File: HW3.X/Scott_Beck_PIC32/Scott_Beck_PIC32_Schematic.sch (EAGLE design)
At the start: 22 parts, among them J1 USB-MB-H

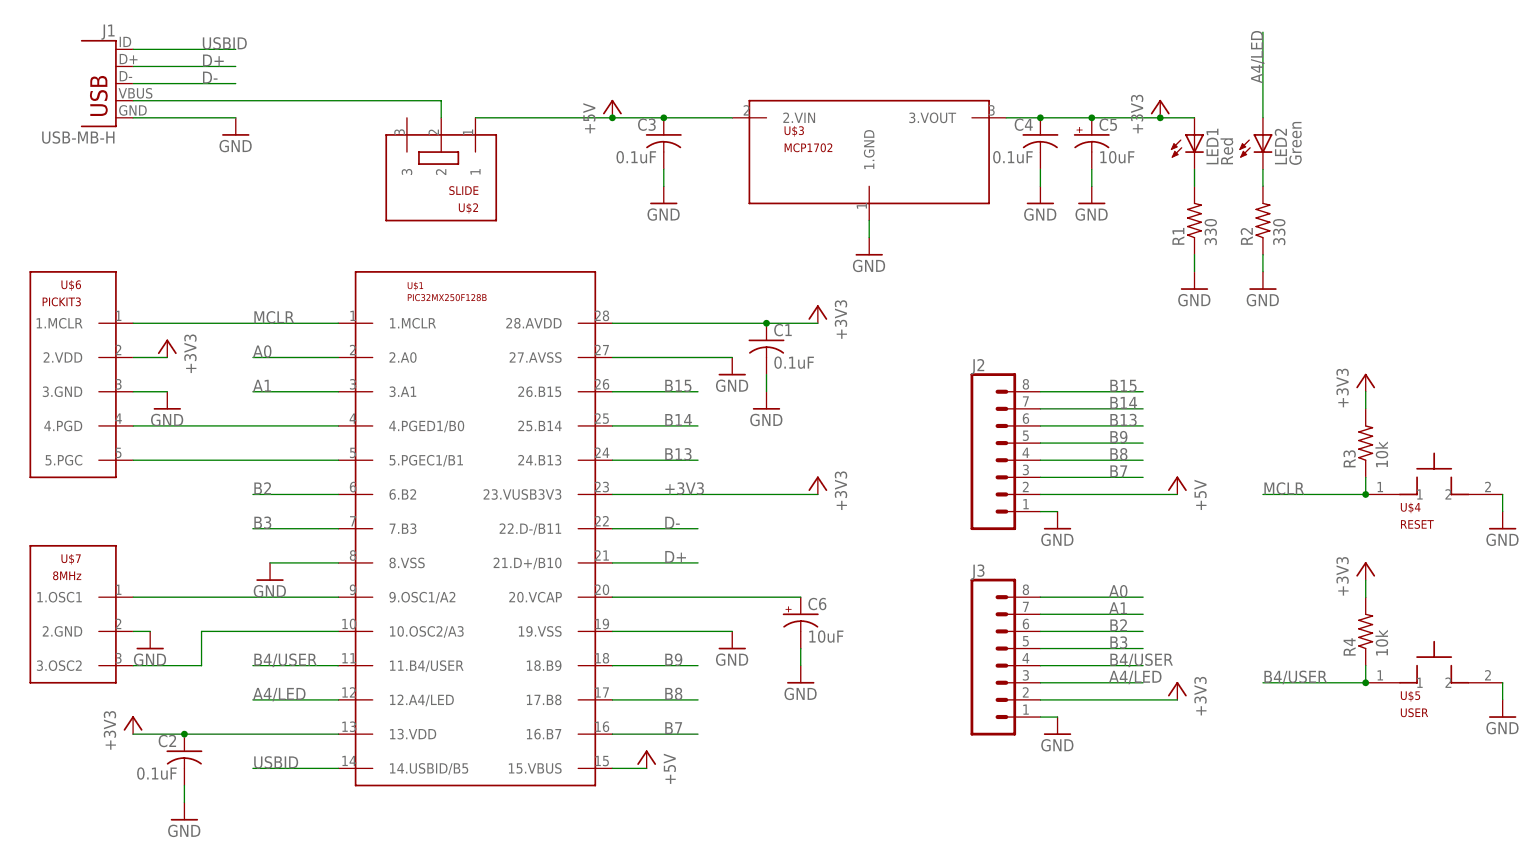
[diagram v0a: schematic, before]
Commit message: Updated Board
Began Design, Replaced res/cap with surface mounts.
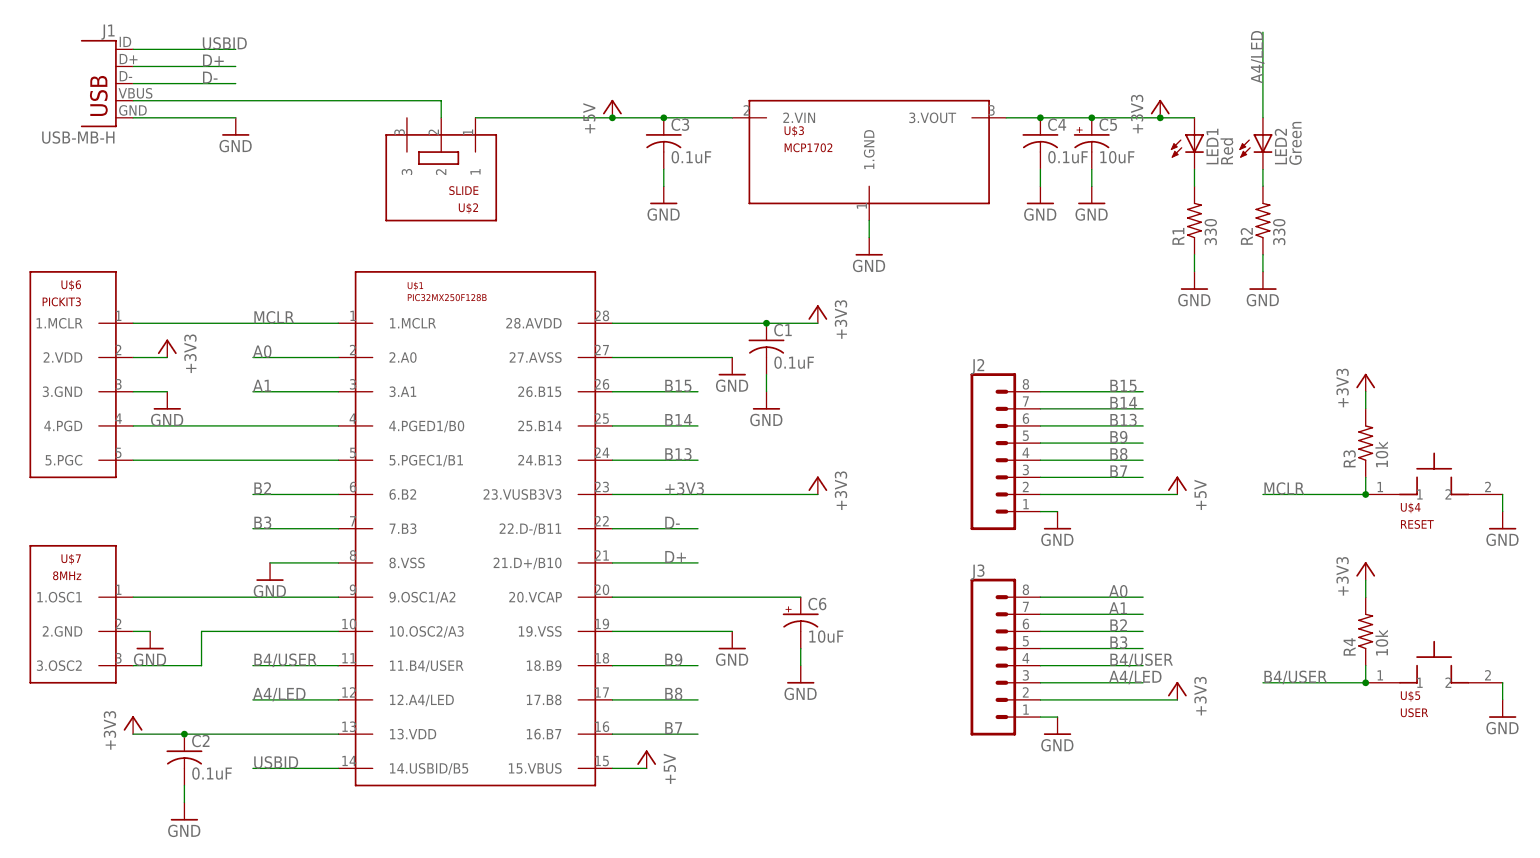
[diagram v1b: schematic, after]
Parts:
- C1, C2, C3, C4: device Scott_Beck_PIC32_Library:C-US025-025X050 -> resistor:C-USC0603
- R1, R2, R3, R4: device Scott_Beck_PIC32_Library:R-US_0207/10 -> resistor:R-US_R0603
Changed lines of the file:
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@@
 <part name="U$4" library="Scott_Beck_PIC32_Library" deviceset="PB" device="" value="RESET"/>
 <part name="U$5" library="Scott_Beck_PIC32_Library" deviceset="PB" device="" value="USER"/>
-<part name="R1" library="Scott_Beck_PIC32_Library" deviceset="R-US_" device="0207/10" value="330"/>
-<part name="R2" library="Scott_Beck_PIC32_Library" deviceset="R-US_" device="0207/10" value="330"/>
-<part name="R3" library="Scott_Beck_PIC32_Library" deviceset="R-US_" device="0207/10" value="10k"/>
-<part name="R4" library="Scott_Beck_PIC32_Library" deviceset="R-US_" device="0207/10" value="10k"/>
-<part name="C1" library="Scott_Beck_PIC32_Library" deviceset="C-US" device="025-025X050" value="0.1uF"/>
-<part name="C2" library="Scott_Beck_PIC32_Library" deviceset="C-US" device="025-025X050" value="0.1uF"/>
-<part name="C3" library="Scott_Beck_PIC32_Library" deviceset="C-US" device="025-025X050" value="0.1uF"/>
-<part name="C4" library="Scott_Beck_PIC32_Library" deviceset="C-US" device="025-025X050" value="0.1uF"/>
 <part name="C5" library="Scott_Beck_PIC32_Library" deviceset="CPOL-US" device="B45181B" value="10uF"/>
 <part name="C6" library="Scott_Beck_PIC32_Library" deviceset="CPOL-US" device="B45181B" value="10uF"/>
@@
 <part name="+3V8" library="Scott_Beck_PIC32_Library" deviceset="+3V3" device=""/>
 <part name="GND19" library="Scott_Beck_PIC32_Library" deviceset="GND" device=""/>
+<part name="R1" library="resistor" deviceset="R-US_" device="R0603" value="330"/>
+<part name="R3" library="resistor" deviceset="R-US_" device="R0603" value="10k"/>
+<part name="R2" library="resistor" deviceset="R-US_" device="R0603" value="330"/>
+<part name="R4" library="resistor" deviceset="R-US_" device="R0603" value="10k"/>
+<part name="C1" library="resistor" deviceset="C-US" device="C0603" value="0.1uF"/>
+<part name="C2" library="resistor" deviceset="C-US" device="C0603" value="0.1uF"/>
+<part name="C3" library="resistor" deviceset="C-US" device="C0603" value="0.1uF"/>
+<part name="C4" library="resistor" deviceset="C-US" device="C0603" value="0.1uF"/>
 </parts>
 <sheets>
@@
 <instance part="U$4" gate="G$1" x="76.2" y="12.7"/>
 <instance part="U$5" gate="G$1" x="76.2" y="-15.24"/>
-<instance part="R1" gate="G$1" x="40.64" y="53.34" rot="R90"/>
-<instance part="R2" gate="G$1" x="50.8" y="53.34" rot="R90"/>
-<instance part="R3" gate="G$1" x="66.04" y="20.32" rot="R90"/>
-<instance part="R4" gate="G$1" x="66.04" y="-7.62" rot="R90"/>
-<instance part="C1" gate="G$1" x="-22.86" y="35.56"/>
-<instance part="C2" gate="G$1" x="-109.22" y="-25.4" rot="MR0"/>
-<instance part="C3" gate="G$1" x="-38.1" y="66.04" rot="MR0"/>
-<instance part="C4" gate="G$1" x="17.78" y="66.04" rot="MR0"/>
 <instance part="C5" gate="G$1" x="25.4" y="66.04"/>
 <instance part="C6" gate="G$1" x="-17.78" y="-5.08"/>
@@
 <instance part="+3V8" gate="G$1" x="66.04" y="2.54"/>
 <instance part="GND19" gate="1" x="50.8" y="43.18"/>
+<instance part="R1" gate="G$1" x="40.64" y="53.34" rot="R90"/>
+<instance part="R3" gate="G$1" x="66.04" y="20.32" rot="R90"/>
+<instance part="R2" gate="G$1" x="50.8" y="53.34" rot="R90"/>
+<instance part="R4" gate="G$1" x="66.04" y="-7.62" rot="R90"/>
+<instance part="C1" gate="G$1" x="-22.86" y="35.56"/>
+<instance part="C2" gate="G$1" x="-109.22" y="-25.4"/>
+<instance part="C3" gate="G$1" x="-38.1" y="66.04"/>
+<instance part="C4" gate="G$1" x="17.78" y="66.04"/>
 </instances>
 <busses>
@@
 <net name="GND" class="0">
 <segment>
-<pinref part="C1" gate="G$1" pin="2"/>
 <pinref part="GND8" gate="1" pin="GND"/>
 <wire x1="-22.86" y1="27.94" x2="-22.86" y2="30.48" width="0.1524" layer="91"/>
+<pinref part="C1" gate="G$1" pin="2"/>
 </segment>
 <segment>
@@
 </segment>
 <segment>
-<pinref part="C3" gate="G$1" pin="2"/>
 <pinref part="GND10" gate="1" pin="GND"/>
 <wire x1="-38.1" y1="60.96" x2="-38.1" y2="58.42" width="0.1524" layer="91"/>
+<pinref part="C3" gate="G$1" pin="2"/>
 </segment>
 <segment>
@@
 </segment>
 <segment>
-<pinref part="C4" gate="G$1" pin="2"/>
 <pinref part="GND11" gate="1" pin="GND"/>
 <wire x1="17.78" y1="60.96" x2="17.78" y2="58.42" width="0.1524" layer="91"/>
+<pinref part="C4" gate="G$1" pin="2"/>
 </segment>
 <segment>
@@
 </segment>
 <segment>
-<pinref part="R1" gate="G$1" pin="1"/>
 <pinref part="GND14" gate="1" pin="GND"/>
 <wire x1="40.64" y1="48.26" x2="40.64" y2="45.72" width="0.1524" layer="91"/>
+<pinref part="R1" gate="G$1" pin="1"/>
 </segment>
 <segment>
@@
 </segment>
 <segment>
-<pinref part="C2" gate="G$1" pin="2"/>
 <pinref part="GND4" gate="1" pin="GND"/>
 <wire x1="-109.22" y1="-30.48" x2="-109.22" y2="-33.02" width="0.1524" layer="91"/>
+<pinref part="C2" gate="G$1" pin="2"/>
 </segment>
 <segment>
@@
 </segment>
 <segment>
-<pinref part="R2" gate="G$1" pin="1"/>
 <pinref part="GND19" gate="1" pin="GND"/>
 <wire x1="50.8" y1="48.26" x2="50.8" y2="45.72" width="0.1524" layer="91"/>
+<pinref part="R2" gate="G$1" pin="1"/>
 </segment>
 </net>
@@
 <pinref part="P+1" gate="1" pin="+5V"/>
 <wire x1="-66.04" y1="68.58" x2="-45.72" y2="68.58" width="0.1524" layer="91"/>
-<pinref part="C3" gate="G$1" pin="1"/>
-<wire x1="-38.1" y1="68.58" x2="-45.72" y2="68.58" width="0.1524" layer="91"/>
 <junction x="-45.72" y="68.58"/>
 <pinref part="U$3" gate="G$1" pin="2.VIN"/>
+<wire x1="-45.72" y1="68.58" x2="-38.1" y2="68.58" width="0.1524" layer="91"/>
+<pinref part="C3" gate="G$1" pin="1"/>
 <wire x1="-38.1" y1="68.58" x2="-27.94" y2="68.58" width="0.1524" layer="91"/>
 <junction x="-38.1" y="68.58"/>
@@
 <segment>
 <pinref part="U$3" gate="G$1" pin="3.VOUT"/>
-<pinref part="C4" gate="G$1" pin="1"/>
+<pinref part="C5" gate="G$1" pin="+"/>
 <wire x1="12.7" y1="68.58" x2="17.78" y2="68.58" width="0.1524" layer="91"/>
-<pinref part="C5" gate="G$1" pin="+"/>
+<pinref part="+3V5" gate="G$1" pin="+3V3"/>
 <wire x1="17.78" y1="68.58" x2="25.4" y2="68.58" width="0.1524" layer="91"/>
-<junction x="17.78" y="68.58"/>
-<pinref part="+3V5" gate="G$1" pin="+3V3"/>
 <wire x1="25.4" y1="68.58" x2="35.56" y2="68.58" width="0.1524" layer="91"/>
 <junction x="25.4" y="68.58"/>
@@
 <wire x1="35.56" y1="68.58" x2="40.64" y2="68.58" width="0.1524" layer="91"/>
 <junction x="35.56" y="68.58"/>
+<pinref part="C4" gate="G$1" pin="1"/>
+<junction x="17.78" y="68.58"/>
 </segment>
 <segment>
 <pinref part="+3V1" gate="G$1" pin="+3V3"/>
+<pinref part="U$1" gate="G$1" pin="13.VDD"/>
+<wire x1="-116.84" y1="-22.86" x2="-109.22" y2="-22.86" width="0.1524" layer="91"/>
 <pinref part="C2" gate="G$1" pin="1"/>
-<wire x1="-116.84" y1="-22.86" x2="-109.22" y2="-22.86" width="0.1524" layer="91"/>
-<pinref part="U$1" gate="G$1" pin="13.VDD"/>
 <wire x1="-109.22" y1="-22.86" x2="-86.36" y2="-22.86" width="0.1524" layer="91"/>
 <junction x="-109.22" y="-22.86"/>
@@
 <segment>
 <pinref part="U$1" gate="G$1" pin="28.AVDD"/>
-<pinref part="C1" gate="G$1" pin="1"/>
 <wire x1="-45.72" y1="38.1" x2="-22.86" y2="38.1" width="0.1524" layer="91"/>
 <pinref part="+3V2" gate="G$1" pin="+3V3"/>
+<pinref part="C1" gate="G$1" pin="1"/>
 <wire x1="-22.86" y1="38.1" x2="-15.24" y2="38.1" width="0.1524" layer="91"/>
 <junction x="-22.86" y="38.1"/>
@@
 </segment>
 <segment>
-<pinref part="R3" gate="G$1" pin="2"/>
 <pinref part="+3V4" gate="G$1" pin="+3V3"/>
 <wire x1="66.04" y1="25.4" x2="66.04" y2="27.94" width="0.1524" layer="91"/>
+<pinref part="R3" gate="G$1" pin="2"/>
 </segment>
 <segment>
 <pinref part="+3V8" gate="G$1" pin="+3V3"/>
+<wire x1="66.04" y1="0" x2="66.04" y2="-2.54" width="0.1524" layer="91"/>
 <pinref part="R4" gate="G$1" pin="2"/>
-<wire x1="66.04" y1="0" x2="66.04" y2="-2.54" width="0.1524" layer="91"/>
 </segment>
 <segment>
@@
 <segment>
 <pinref part="LED1" gate="G$1" pin="C"/>
+<wire x1="40.64" y1="60.96" x2="40.64" y2="58.42" width="0.1524" layer="91"/>
 <pinref part="R1" gate="G$1" pin="2"/>
-<wire x1="40.64" y1="60.96" x2="40.64" y2="58.42" width="0.1524" layer="91"/>
 </segment>
 </net>
@@
 <segment>
 <pinref part="U$4" gate="G$1" pin="1"/>
-<pinref part="R3" gate="G$1" pin="1"/>
 <wire x1="66.04" y1="12.7" x2="66.04" y2="15.24" width="0.1524" layer="91"/>
 <wire x1="66.04" y1="12.7" x2="50.8" y2="12.7" width="0.1524" layer="91"/>
 <junction x="66.04" y="12.7"/>
 <label x="50.8" y="12.7" size="1.778" layer="95"/>
+<pinref part="R3" gate="G$1" pin="1"/>
 </segment>
 </net>
@@
 </segment>
 <segment>
-<pinref part="R4" gate="G$1" pin="1"/>
 <pinref part="U$5" gate="G$1" pin="1"/>
 <wire x1="66.04" y1="-12.7" x2="66.04" y2="-15.24" width="0.1524" layer="91"/>
@@
 <junction x="66.04" y="-15.24"/>
 <label x="50.8" y="-15.24" size="1.778" layer="95"/>
+<pinref part="R4" gate="G$1" pin="1"/>
 </segment>
 <segment>
@@
 <segment>
 <pinref part="LED2" gate="G$1" pin="C"/>
+<wire x1="50.8" y1="60.96" x2="50.8" y2="58.42" width="0.1524" layer="91"/>
 <pinref part="R2" gate="G$1" pin="2"/>
-<wire x1="50.8" y1="60.96" x2="50.8" y2="58.42" width="0.1524" layer="91"/>
-</segment>
-</net>
+</segment>
+</net>

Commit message: First Complete Board
First Draft of Completed Board
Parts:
- C5, C6: device Scott_Beck_PIC32_Library:CPOL-USB45181B -> resistor:C-USC0603
- LED1, LED2: device led:LED3MM -> led:LEDSML0603
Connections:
- net +3V3: now also C5.1; no longer C5.+
- net GND: now also C5.2, C6.2; no longer C5.-, C6.-
- net N$5: now also C6.1; no longer C6.+
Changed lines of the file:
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@@
 <part name="U$2" library="Scott_Beck_PIC32_Library" deviceset="SLIDE" device=""/>
 <part name="U$3" library="Scott_Beck_PIC32_Library" deviceset="MCP1702" device=""/>
-<part name="LED1" library="led" deviceset="LED" device="3MM" value="Red"/>
-<part name="LED2" library="led" deviceset="LED" device="3MM" value="Green"/>
 <part name="U$4" library="Scott_Beck_PIC32_Library" deviceset="PB" device="" value="RESET"/>
 <part name="U$5" library="Scott_Beck_PIC32_Library" deviceset="PB" device="" value="USER"/>
-<part name="C5" library="Scott_Beck_PIC32_Library" deviceset="CPOL-US" device="B45181B" value="10uF"/>
-<part name="C6" library="Scott_Beck_PIC32_Library" deviceset="CPOL-US" device="B45181B" value="10uF"/>
 <part name="J2" library="Scott_Beck_PIC32_Library" deviceset="CONN_08" device="&quot;"/>
 <part name="J3" library="Scott_Beck_PIC32_Library" deviceset="CONN_08" device="&quot;"/>
@@
 <part name="C3" library="resistor" deviceset="C-US" device="C0603" value="0.1uF"/>
 <part name="C4" library="resistor" deviceset="C-US" device="C0603" value="0.1uF"/>
+<part name="C5" library="resistor" deviceset="C-US" device="C0603" value="10uF"/>
+<part name="C6" library="resistor" deviceset="C-US" device="C0603" value="10uF"/>
+<part name="LED1" library="led" deviceset="LED" device="SML0603" value="Red"/>
+<part name="LED2" library="led" deviceset="LED" device="SML0603" value="Green"/>
 </parts>
 <sheets>
 <sheet>
 <plain>
+<wire x1="23.622" y1="67.564" x2="23.622" y2="66.548" width="0.1524" layer="94"/>
+<wire x1="23.114" y1="67.056" x2="24.13" y2="67.056" width="0.1524" layer="94"/>
+<wire x1="-19.558" y1="-3.556" x2="-19.558" y2="-4.572" width="0.1524" layer="94"/>
+<wire x1="-20.066" y1="-4.064" x2="-19.05" y2="-4.064" width="0.1524" layer="94"/>
 </plain>
 <instances>
@@
 <instance part="U$2" gate="G$1" x="-71.12" y="63.5" rot="R180"/>
 <instance part="U$3" gate="G$1" x="-7.62" y="68.58"/>
-<instance part="LED1" gate="G$1" x="40.64" y="66.04"/>
-<instance part="LED2" gate="G$1" x="50.8" y="66.04"/>
 <instance part="U$4" gate="G$1" x="76.2" y="12.7"/>
 <instance part="U$5" gate="G$1" x="76.2" y="-15.24"/>
-<instance part="C5" gate="G$1" x="25.4" y="66.04"/>
-<instance part="C6" gate="G$1" x="-17.78" y="-5.08"/>
 <instance part="J2" gate="G$1" x="12.7" y="17.78"/>
 <instance part="J3" gate="G$1" x="12.7" y="-12.7"/>
@@
 <instance part="C3" gate="G$1" x="-38.1" y="66.04"/>
 <instance part="C4" gate="G$1" x="17.78" y="66.04"/>
+<instance part="C5" gate="G$1" x="25.4" y="66.04"/>
+<instance part="C6" gate="G$1" x="-17.78" y="-5.08"/>
+<instance part="LED1" gate="G$1" x="40.64" y="66.04"/>
+<instance part="LED2" gate="G$1" x="50.8" y="66.04"/>
 </instances>
 <busses>
@@
 </segment>
 <segment>
-<pinref part="C5" gate="G$1" pin="-"/>
 <pinref part="GND15" gate="1" pin="GND"/>
 <wire x1="25.4" y1="60.96" x2="25.4" y2="58.42" width="0.1524" layer="91"/>
+<pinref part="C5" gate="G$1" pin="2"/>
 </segment>
 <segment>
@@
 </segment>
 <segment>
-<pinref part="C6" gate="G$1" pin="-"/>
 <pinref part="GND5" gate="1" pin="GND"/>
 <wire x1="-17.78" y1="-10.16" x2="-17.78" y2="-12.7" width="0.1524" layer="91"/>
+<pinref part="C6" gate="G$1" pin="2"/>
 </segment>
 <segment>
@@
 <segment>
 <pinref part="U$3" gate="G$1" pin="3.VOUT"/>
-<pinref part="C5" gate="G$1" pin="+"/>
 <wire x1="12.7" y1="68.58" x2="17.78" y2="68.58" width="0.1524" layer="91"/>
 <pinref part="+3V5" gate="G$1" pin="+3V3"/>
 <wire x1="17.78" y1="68.58" x2="25.4" y2="68.58" width="0.1524" layer="91"/>
 <wire x1="25.4" y1="68.58" x2="35.56" y2="68.58" width="0.1524" layer="91"/>
-<junction x="25.4" y="68.58"/>
-<pinref part="LED1" gate="G$1" pin="A"/>
 <wire x1="35.56" y1="68.58" x2="40.64" y2="68.58" width="0.1524" layer="91"/>
 <junction x="35.56" y="68.58"/>
 <pinref part="C4" gate="G$1" pin="1"/>
 <junction x="17.78" y="68.58"/>
+<pinref part="C5" gate="G$1" pin="1"/>
+<junction x="25.4" y="68.58"/>
+<pinref part="LED1" gate="G$1" pin="A"/>
 </segment>
 <segment>
@@
 <net name="N$3" class="0">
 <segment>
-<pinref part="LED1" gate="G$1" pin="C"/>
 <wire x1="40.64" y1="60.96" x2="40.64" y2="58.42" width="0.1524" layer="91"/>
 <pinref part="R1" gate="G$1" pin="2"/>
+<pinref part="LED1" gate="G$1" pin="C"/>
 </segment>
 </net>
@@
 <segment>
 <pinref part="U$1" gate="G$1" pin="20.VCAP"/>
-<pinref part="C6" gate="G$1" pin="+"/>
 <wire x1="-45.72" y1="-2.54" x2="-17.78" y2="-2.54" width="0.1524" layer="91"/>
+<pinref part="C6" gate="G$1" pin="1"/>
 </segment>
 </net>
@@
 </segment>
 <segment>
-<pinref part="LED2" gate="G$1" pin="A"/>
 <wire x1="50.8" y1="68.58" x2="50.8" y2="81.28" width="0.1524" layer="91"/>
 <label x="50.8" y="73.66" size="1.778" layer="95" rot="R90"/>
+<pinref part="LED2" gate="G$1" pin="A"/>
 </segment>
 </net>
@@
 <net name="N$6" class="0">
 <segment>
-<pinref part="LED2" gate="G$1" pin="C"/>
 <wire x1="50.8" y1="60.96" x2="50.8" y2="58.42" width="0.1524" layer="91"/>
 <pinref part="R2" gate="G$1" pin="2"/>
-</segment>
-</net>
+<pinref part="LED2" gate="G$1" pin="C"/>
+</segment>
+</net>

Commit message: Semi-Finalized Board
Pre-Final Checks
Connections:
- net N$7 renamed PGD
- net N$8 renamed PGC
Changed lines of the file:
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@@
 </segment>
 </net>
-<net name="N$7" class="0">
+<net name="PGD" class="0">
 <segment>
 <pinref part="U$6" gate="G$1" pin="4.PGD"/>
@@
 </segment>
 </net>
-<net name="N$8" class="0">
+<net name="PGC" class="0">
 <segment>
 <pinref part="U$6" gate="G$1" pin="5.PGC"/>
